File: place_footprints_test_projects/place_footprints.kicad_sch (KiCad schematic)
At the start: 1 part

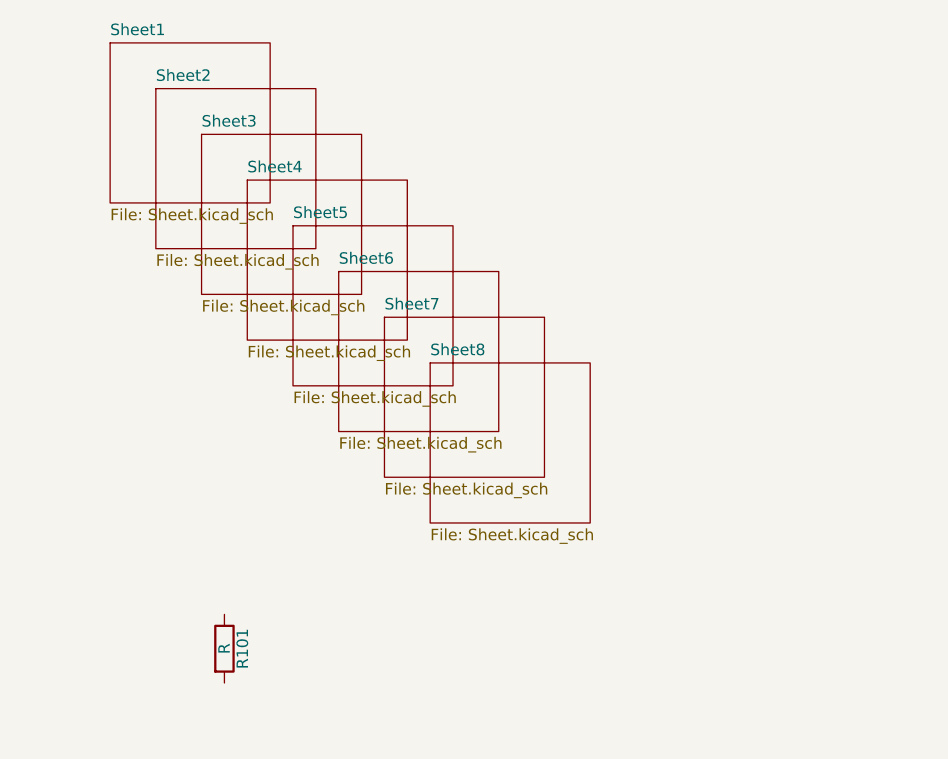
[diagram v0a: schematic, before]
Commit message: fix the matrix layout to support anchor footprint to be in the middle of the list
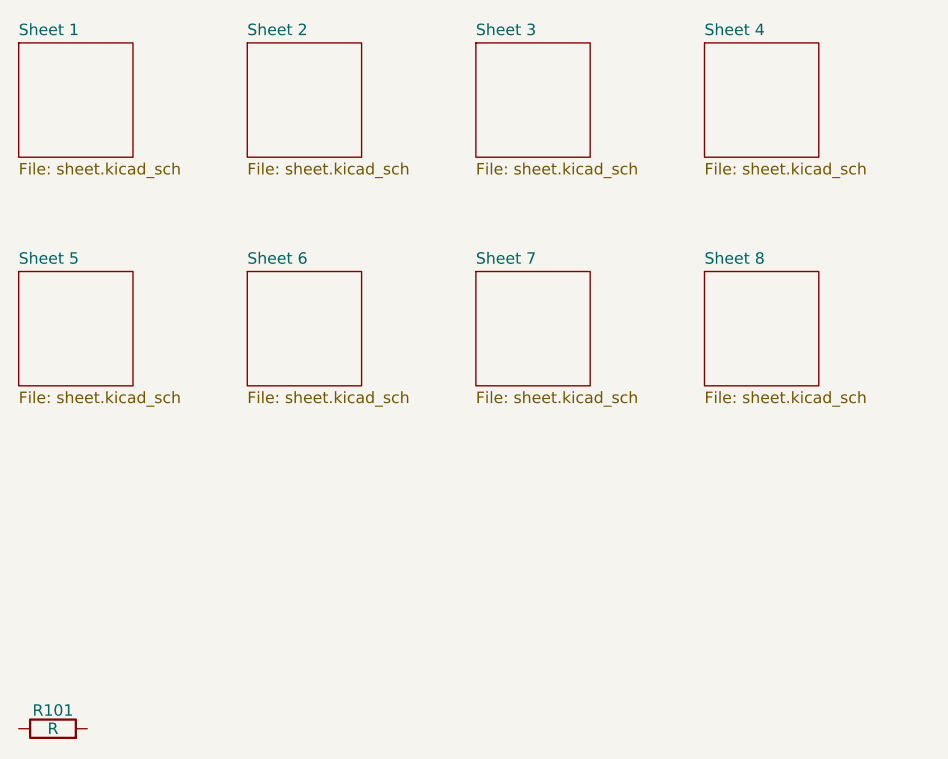
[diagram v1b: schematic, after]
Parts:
- R101: footprint Resistor_SMD:R_1210_3225Metric_Pad1.30x2.65mm_HandSolder -> Resistor_SMD:R_1206_3216Metric
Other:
- removed sheet Sheet1
- removed sheet Sheet2
- removed sheet Sheet3
- removed sheet Sheet4
- removed sheet Sheet5
- removed sheet Sheet6
- removed sheet Sheet7
- removed sheet Sheet8
- added sheet Sheet 1 (sheet.kicad_sch)
- added sheet Sheet 2 (sheet.kicad_sch)
- added sheet Sheet 3 (sheet.kicad_sch)
- added sheet Sheet 4 (sheet.kicad_sch)
- added sheet Sheet 5 (sheet.kicad_sch)
- added sheet Sheet 6 (sheet.kicad_sch)
- added sheet Sheet 7 (sheet.kicad_sch)
- added sheet Sheet 8 (sheet.kicad_sch)
